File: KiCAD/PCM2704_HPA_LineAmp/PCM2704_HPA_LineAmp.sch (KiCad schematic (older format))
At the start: 10 parts, among them J1 PCM2704Board, U1 NJM4580

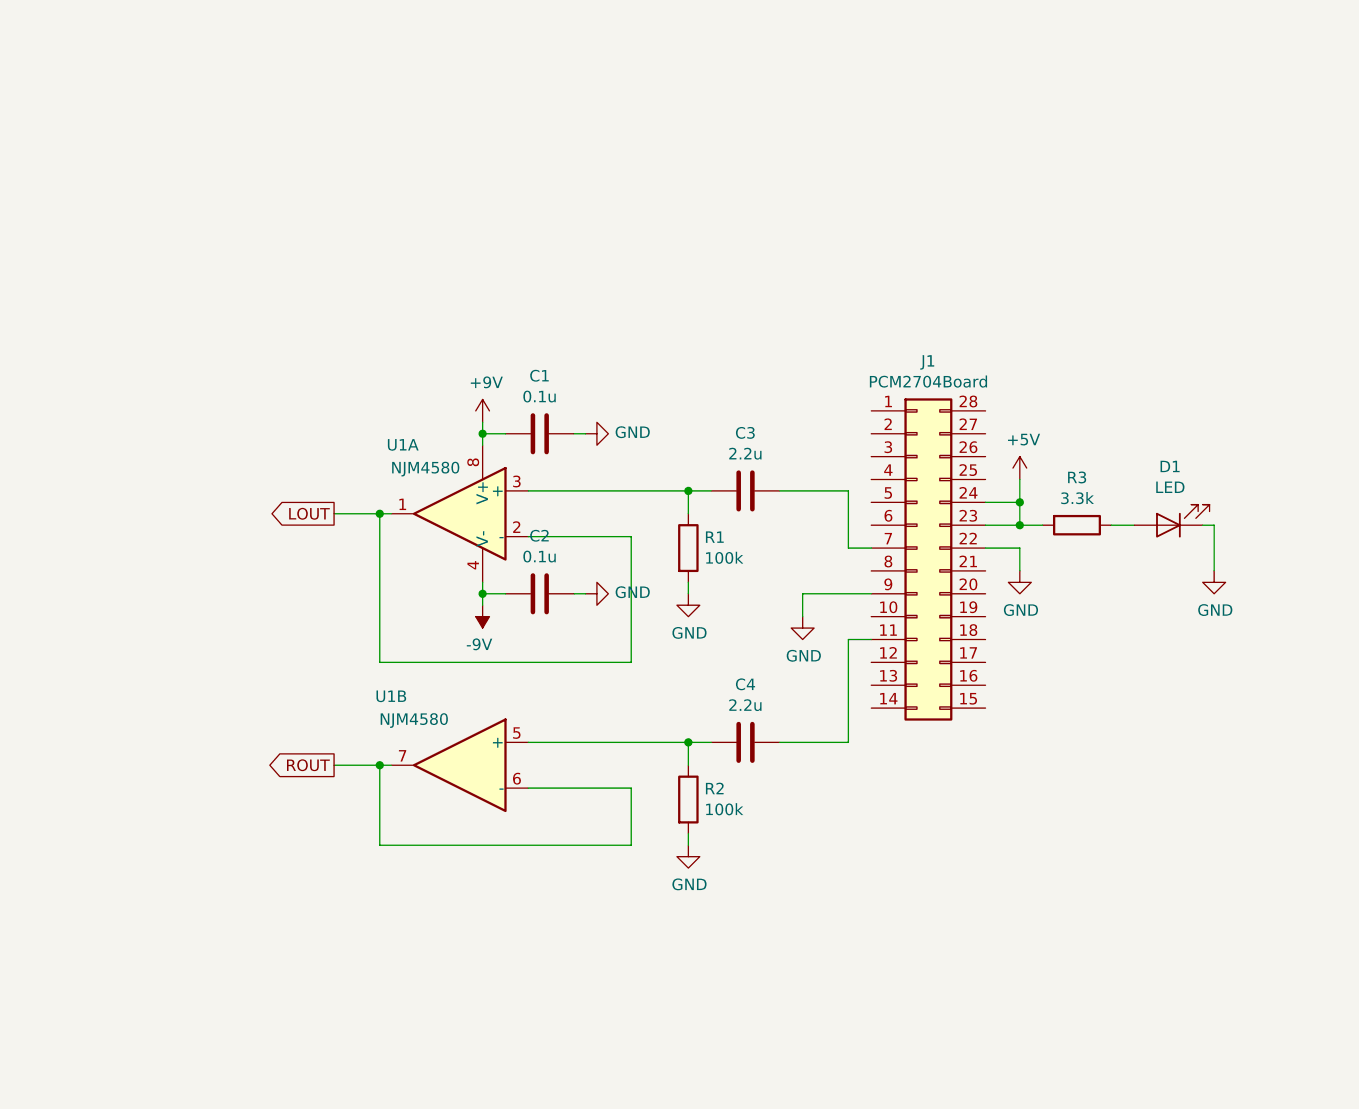
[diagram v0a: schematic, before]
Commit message: Add: PCM2704_LineAmp
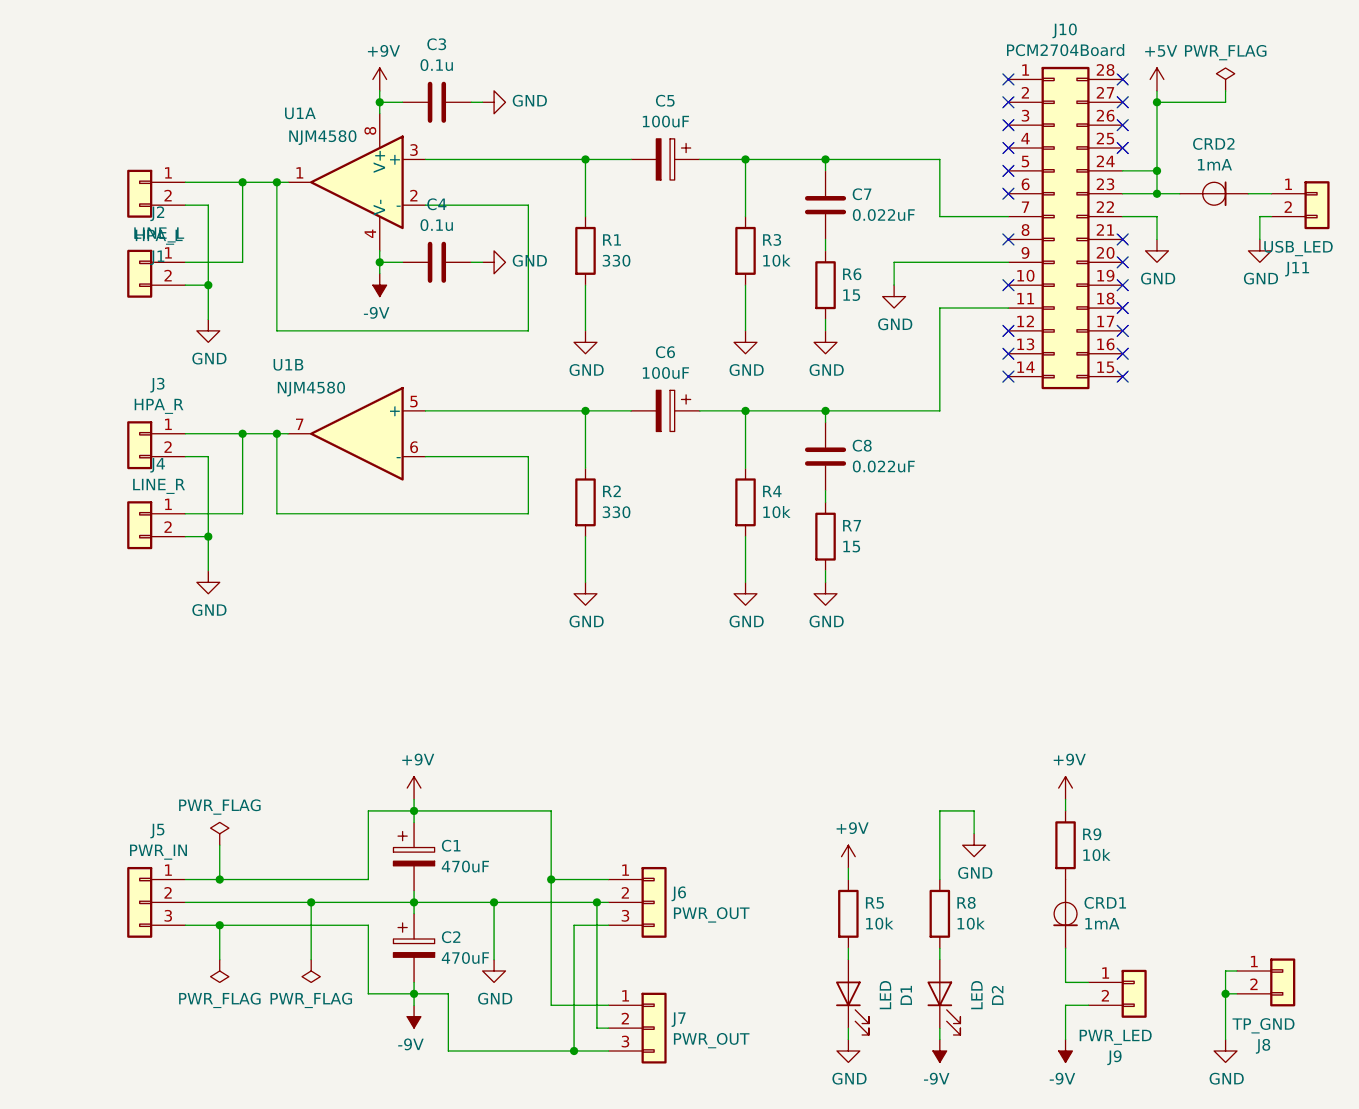
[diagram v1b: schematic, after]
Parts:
- removed C3, C4: 2.2u, symbol Device:C
- added C1, C2: 470uF, Capacitor_THT:CP_Radial_D10.0mm_P5.00mm, symbol Device:CP
- added C5, C6: 100uF, Capacitor_THT:CP_Radial_D8.0mm_P5.00mm, symbol Device:CP
- added C7, C8: 0.022uF, Capacitor_THT:C_Rect_L7.0mm_W2.0mm_P5.00mm, symbol Device:C
- added CRD1, CRD2: 1mA, Diode_THT:D_A-405_P7.62mm_Horizontal, symbol mylib:CRD
- added D2: LED, LED_THT:LED_D3.0mm, symbol Device:LED
- added J1: HPA_L, Connector_JST:JST_XH_B2B-XH-A_1x02_P2.50mm_Vertical, symbol Connector_Generic:Conn_01x02
- added J11: USB_LED, Connector_PinHeader_2.54mm:PinHeader_1x02_P2.54mm_Vertical, symbol Connector_Generic:Conn_01x02
- added J2: LINE_L, Connector_JST:JST_XH_B2B-XH-A_1x02_P2.50mm_Vertical, symbol Connector_Generic:Conn_01x02
- added J3: HPA_R, Connector_JST:JST_XH_B2B-XH-A_1x02_P2.50mm_Vertical, symbol Connector_Generic:Conn_01x02
- added J4: LINE_R, Connector_JST:JST_XH_B2B-XH-A_1x02_P2.50mm_Vertical, symbol Connector_Generic:Conn_01x02
- added J5: PWR_IN, Connector_JST:JST_XH_B3B-XH-A_1x03_P2.50mm_Vertical, symbol Connector_Generic:Conn_01x03
- added J6, J7: PWR_OUT, Connector_JST:JST_XH_B3B-XH-A_1x03_P2.50mm_Vertical, symbol Connector_Generic:Conn_01x03
- added J8: TP_GND, Connector_PinHeader_2.54mm:PinHeader_1x02_P2.54mm_Vertical, symbol Connector_Generic:Conn_01x02
- added J9: PWR_LED, Connector_PinHeader_2.54mm:PinHeader_1x02_P2.54mm_Vertical, symbol Connector_Generic:Conn_01x02
- added R4, R5, R8, R9: 10k, Resistor_THT:R_Axial_DIN0204_L3.6mm_D1.6mm_P7.62mm_Horizontal, symbol Device:R
- added R6, R7: 15, Resistor_THT:R_Axial_DIN0204_L3.6mm_D1.6mm_P7.62mm_Horizontal, symbol Device:R
- C3: renamed from C1; footprint (none) -> Capacitor_THT:C_Disc_D3.0mm_W1.6mm_P2.50mm
- C4: renamed from C2; footprint (none) -> Capacitor_THT:C_Disc_D3.0mm_W1.6mm_P2.50mm
- D1: footprint (none) -> LED_THT:LED_D3.0mm
- J10: renamed from J1; footprint (none) -> Package_DIP:DIP-28_W15.24mm
- R1, R2: value 100k -> 330; footprint (none) -> Resistor_THT:R_Axial_DIN0204_L3.6mm_D1.6mm_P7.62mm_Horizontal
- R3: value 3.3k -> 10k; footprint (none) -> Resistor_THT:R_Axial_DIN0204_L3.6mm_D1.6mm_P7.62mm_Horizontal
- U1: footprint (none) -> Package_DIP:DIP-8_W7.62mm_Socket
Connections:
- net +5V: now also CRD2.2 (A); no longer R3.2
- net +9V: now also C1.1, J5.1 (Pin_1), J6.1 (Pin_1), J7.1 (Pin_1), R5.1, R9.1
- net -9V: now also C2.2, D2.1 (K), J5.3 (Pin_3), J6.3 (Pin_3), J7.3 (Pin_3), J9.2 (Pin_2)
- net GND: now also R3.2, C1.2, C2.1, J1.2 (Pin_2), J11.2 (Pin_2), J2.2 (Pin_2), J3.2 (Pin_2), J4.2 (Pin_2), J5.2 (Pin_2), J6.2 (Pin_2), J7.2 (Pin_2), J8.1 (Pin_1), J8.2 (Pin_2), R4.2, R6.2, R7.2, R8.1
- net at J10.11 (Pin_11): now also C6.1, C8.1, R4.1
- net at J10.7 (Pin_7): now also R3.1, C5.1, C7.1
- net at D1.2 (A): now also R5.2; no longer R3.1
- net at R1.1, U1.3 (+): now also C5.2
- net at R2.1, U1.5 (+): now also C6.2
- net LOUT: no longer names the net of U1.1, U1.2 (-)
- net LOUT: now also J1.1 (Pin_1), J2.1 (Pin_1)
- net ROUT: no longer names the net of U1.6 (-), U1.7
- net ROUT: now also J3.1 (Pin_1), J4.1 (Pin_1)
- new net: C7.2, R6.1
- new net: C8.2, R7.1
- new net: CRD1.1 (K), J9.1 (Pin_1)
- new net: CRD1.2 (A), R9.2
- new net: D2.2 (A), R8.2
- new net: CRD2.1 (K), J11.1 (Pin_1)
- no-connect marks 0 -> 22
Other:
- moved on the sheet: C3, C4, J10, R1, R2, U1A, U1B

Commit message: Update: PCM2704_HPA_LineAmp board design
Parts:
- removed J5: PWR_IN, Connector_JST:JST_XH_B3B-XH-A_1x03_P2.50mm_Vertical, symbol Connector_Generic:Conn_01x03
- added J12: PWR-, Connector_JST:JST_XH_B2B-XH-A_1x02_P2.50mm_Vertical, symbol Connector_Generic:Conn_01x02
- added J5: PWR+, Connector_JST:JST_XH_B2B-XH-A_1x02_P2.50mm_Vertical, symbol Connector_Generic:Conn_01x02
- C4: footprint Capacitor_THT:C_Disc_D3.0mm_W1.6mm_P2.50mm -> Capacitor_THT:C_Disc_D4.3mm_W1.9mm_P5.00mm
- C5, C6: footprint Capacitor_THT:CP_Radial_D8.0mm_P5.00mm -> Capacitor_THT:CP_Radial_D7.5mm_P2.50mm
- CRD1, CRD2: value 1mA -> 10mA; footprint Diode_THT:D_A-405_P7.62mm_Horizontal -> Diode_THT:D_DO-35_SOD27_P7.62mm_Horizontal
- R1, R2: value 330 -> 3k3
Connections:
- net +9V: now also D1.2 (A), J5.1 (Pin_1); no longer R5.1
- net -9V: now also J12.2 (Pin_2)
- net GND: now also R5.2, J12.1 (Pin_1), J5.2 (Pin_2); no longer D1.1 (K)
- net at C5.2, R1.1: now also U1.5 (+); no longer U1.3 (+)
- net at C6.2, R2.1: now also U1.3 (+); no longer U1.5 (+)
- net at U1.1, U1.2 (-): now also J3.1 (Pin_1), J4.1 (Pin_1); no longer J1.1 (Pin_1), J2.1 (Pin_1)
- net at U1.6 (-), U1.7: now also J1.1 (Pin_1), J2.1 (Pin_1); no longer J3.1 (Pin_1), J4.1 (Pin_1)
- new net: D1.1 (K), R5.1
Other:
- moved on the sheet: D1, R5, U1A, U1B
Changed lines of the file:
@@
 encoding utf-8
 Sheet 1 1
-Title "PCM2074 Line Amp"
-Date "2019-11-06"
+Title "PCM2704 Line Amp"
+Date "2019-11-08"
 Rev "Rev. A"
 Comp "PNPN Manufactory"
@@
 P 4900 2250
 F 0 "R1" H 4970 2296 50  0000 L CNN
-F 1 "330" H 4970 2205 50  0000 L CNN
+F 1 "3k3" H 4970 2205 50  0000 L CNN
 F 2 "Resistor_THT:R_Axial_DIN0204_L3.6mm_D1.6mm_P7.62mm_Horizontal" V 4830 2250 50  0001 C CNN
 F 3 "~" H 4900 2250 50  0001 C CNN
@@
 P 4900 3350
 F 0 "R2" H 4970 3396 50  0000 L CNN
-F 1 "330" H 4970 3305 50  0000 L CNN
+F 1 "3k3" H 4970 3305 50  0000 L CNN
 F 2 "Resistor_THT:R_Axial_DIN0204_L3.6mm_D1.6mm_P7.62mm_Horizontal" V 4830 3350 50  0001 C CNN
 F 3 "~" H 4900 3350 50  0001 C CNN
@@
 L Amplifier_Operational:NJM4580 U1
 U 1 1 5DA27AD1
+P 3900 3050
+F 0 "U1" H 4150 3350 50  0000 C CNN
+F 1 "NJM4580" H 4050 3250 50  0000 C CNN
+F 2 "Package_DIP:DIP-8_W7.62mm_Socket" H 3900 3050 50  0001 C CNN
+F 3 "http://www.njr.com/semicon/PDF/NJM4580_E.pdf" H 3900 3050 50  0001 C CNN
+	1    3900 3050
+	-1   0    0    -1
+$EndComp
+$Comp
+L Amplifier_Operational:NJM4580 U1
+U 2 1 5DA2AA3E
 P 3900 1950
-F 0 "U1" H 4150 2250 50  0000 C CNN
-F 1 "NJM4580" H 4050 2150 50  0000 C CNN
+F 0 "U1" H 4200 2250 50  0000 C CNN
+F 1 "NJM4580" H 4100 2150 50  0000 C CNN
 F 2 "Package_DIP:DIP-8_W7.62mm_Socket" H 3900 1950 50  0001 C CNN
 F 3 "http://www.njr.com/semicon/PDF/NJM4580_E.pdf" H 3900 1950 50  0001 C CNN
-	1    3900 1950
-	-1   0    0    -1
-$EndComp
-$Comp
-L Amplifier_Operational:NJM4580 U1
-U 2 1 5DA2AA3E
-P 3900 3050
-F 0 "U1" H 4200 3350 50  0000 C CNN
-F 1 "NJM4580" H 4100 3250 50  0000 C CNN
-F 2 "Package_DIP:DIP-8_W7.62mm_Socket" H 3900 3050 50  0001 C CNN
-F 3 "http://www.njr.com/semicon/PDF/NJM4580_E.pdf" H 3900 3050 50  0001 C CNN
-	2    3900 3050
+	2    3900 1950
 	-1   0    0    -1
 $EndComp
@@
 F 0 "C4" V 3998 2300 50  0000 C CNN
 F 1 "0.1u" V 4089 2300 50  0000 C CNN
-F 2 "Capacitor_THT:C_Disc_D3.0mm_W1.6mm_P2.50mm" H 4288 2150 50  0001 C CNN
+F 2 "Capacitor_THT:C_Disc_D4.3mm_W1.9mm_P5.00mm" H 4288 2150 50  0001 C CNN
 F 3 "~" H 4250 2300 50  0001 C CNN
 	1    4250 2300
@@
 F 0 "C5" V 4995 1850 50  0000 C CNN
 F 1 "100uF" V 5086 1850 50  0000 C CNN
-F 2 "Capacitor_THT:CP_Radial_D8.0mm_P5.00mm" H 5288 1700 50  0001 C CNN
+F 2 "Capacitor_THT:CP_Radial_D7.5mm_P2.50mm" H 5288 1700 50  0001 C CNN
 F 3 "~" H 5250 1850 50  0001 C CNN
 	1    5250 1850
@@
 F 0 "C6" V 4995 2950 50  0000 C CNN
 F 1 "100uF" V 5086 2950 50  0000 C CNN
-F 2 "Capacitor_THT:CP_Radial_D8.0mm_P5.00mm" H 5288 2800 50  0001 C CNN
+F 2 "Capacitor_THT:CP_Radial_D7.5mm_P2.50mm" H 5288 2800 50  0001 C CNN
 F 3 "~" H 5250 2950 50  0001 C CNN
 	1    5250 2950
@@
 U 1 1 5DC7B009
 P 2950 1950
-F 0 "J1" H 2868 1625 50  0000 C CNN
-F 1 "HPA_L" H 2868 1716 50  0000 C CNN
+F 0 "J1" H 3100 2000 50  0000 C CNN
+F 1 "HPA_L" H 2900 2050 50  0000 C CNN
 F 2 "Connector_JST:JST_XH_B2B-XH-A_1x02_P2.50mm_Vertical" H 2950 1950 50  0001 C CNN
 F 3 "~" H 2950 1950 50  0001 C CNN
@@
 U 1 1 5DC7B7CB
 P 2950 2300
-F 0 "J2" H 2868 2517 50  0000 C CNN
+F 0 "J2" H 3100 2350 50  0000 C CNN
 F 1 "LINE_L" H 2868 2426 50  0000 C CNN
 F 2 "Connector_JST:JST_XH_B2B-XH-A_1x02_P2.50mm_Vertical" H 2950 2300 50  0001 C CNN
@@
 U 1 1 5DC7C23E
 P 2950 3050
-F 0 "J3" H 2868 3267 50  0000 C CNN
+F 0 "J3" H 3100 3100 50  0000 C CNN
 F 1 "HPA_R" H 2868 3176 50  0000 C CNN
 F 2 "Connector_JST:JST_XH_B2B-XH-A_1x02_P2.50mm_Vertical" H 2950 3050 50  0001 C CNN
@@
 U 1 1 5DC7CA20
 P 2950 3400
-F 0 "J4" H 2868 3617 50  0000 C CNN
+F 0 "J4" H 3100 3450 50  0000 C CNN
 F 1 "LINE_R" H 2868 3526 50  0000 C CNN
 F 2 "Connector_JST:JST_XH_B2B-XH-A_1x02_P2.50mm_Vertical" H 2950 3400 50  0001 C CNN
@@
 	7900 2100 7850 2100
 $Comp
-L Connector_Generic:Conn_01x03 J5
-U 1 1 5DD6183F
-P 2950 5100
-F 0 "J5" H 2868 5417 50  0000 C CNN
-F 1 "PWR_IN" H 2868 5326 50  0000 C CNN
-F 2 "Connector_JST:JST_XH_B3B-XH-A_1x03_P2.50mm_Vertical" H 2950 5100 50  0001 C CNN
-F 3 "~" H 2950 5100 50  0001 C CNN
-	1    2950 5100
-	-1   0    0    -1
-$EndComp
-$Comp
 L Connector_Generic:Conn_01x03 J6
 U 1 1 5DD62FDF
@@
 $EndComp
 Wire Wire Line
-	3150 5000 3300 5000
+	2850 5000 3300 5000
 Wire Wire Line
 	3950 5000 3950 4700
@@
 	4150 5150 4150 5100
 Wire Wire Line
-	3150 5200 3300 5200
-Wire Wire Line
 	3950 5200 3950 5500
 Wire Wire Line
@@
 	4150 5500 4150 5450
 Wire Wire Line
-	3150 5100 3700 5100
+	2850 5100 3050 5100
 Connection ~ 4150 5100
 Wire Wire Line
@@
 L Device:LED D1
 U 1 1 5DE43980
-P 6050 5500
-F 0 "D1" H 6043 5245 50  0000 C CNN
-F 1 "LED" H 6043 5336 50  0000 C CNN
-F 2 "LED_THT:LED_D3.0mm" H 6050 5500 50  0001 C CNN
-F 3 "~" H 6050 5500 50  0001 C CNN
-	1    6050 5500
+P 6050 5150
+F 0 "D1" H 6043 4895 50  0000 C CNN
+F 1 "LED" H 6043 4986 50  0000 C CNN
+F 2 "LED_THT:LED_D3.0mm" H 6050 5150 50  0001 C CNN
+F 3 "~" H 6050 5150 50  0001 C CNN
+	1    6050 5150
 	0    -1   -1   0
 $EndComp
@@
 P 7000 5150
 F 0 "CRD1" V 7046 5071 50  0000 R CNN
-F 1 "1mA" V 6955 5071 50  0000 R CNN
-F 2 "Diode_THT:D_A-405_P7.62mm_Horizontal" H 7000 5150 50  0001 C CNN
+F 1 "10mA" V 6955 5071 50  0000 R CNN
+F 2 "Diode_THT:D_DO-35_SOD27_P7.62mm_Horizontal" H 7000 5150 50  0001 C CNN
 F 3 "~" H 7000 5150 50  0001 C CNN
 	1    7000 5150
@@
 P 7650 2000
 F 0 "CRD2" H 7650 1784 50  0000 C CNN
-F 1 "1mA" H 7650 1875 50  0000 C CNN
-F 2 "Diode_THT:D_A-405_P7.62mm_Horizontal" H 7650 2000 50  0001 C CNN
+F 1 "10mA" H 7650 1875 50  0000 C CNN
+F 2 "Diode_THT:D_DO-35_SOD27_P7.62mm_Horizontal" H 7650 2000 50  0001 C CNN
 F 3 "~" H 7650 2000 50  0001 C CNN
 	1    7650 2000
@@
 L Device:R R5
 U 1 1 5DD2A85D
-P 6050 5150
-F 0 "R5" H 6120 5196 50  0000 L CNN
-F 1 "10k" H 6120 5105 50  0000 L CNN
-F 2 "Resistor_THT:R_Axial_DIN0204_L3.6mm_D1.6mm_P7.62mm_Horizontal" V 5980 5150 50  0001 C CNN
-F 3 "~" H 6050 5150 50  0001 C CNN
-	1    6050 5150
+P 6050 5500
+F 0 "R5" H 6120 5546 50  0000 L CNN
+F 1 "10k" H 6120 5455 50  0000 L CNN
+F 2 "Resistor_THT:R_Axial_DIN0204_L3.6mm_D1.6mm_P7.62mm_Horizontal" V 5980 5500 50  0001 C CNN
+F 3 "~" H 6050 5500 50  0001 C CNN
+	1    6050 5500
 	1    0    0    -1
 $EndComp
@@
 	4300 5750 4850 5750
 Connection ~ 4850 5750
+$Comp
+L Connector_Generic:Conn_01x02 J5
+U 1 1 5DCA298D
+P 2650 5000
+F 0 "J5" H 2800 5050 50  0000 C CNN
+F 1 "PWR+" H 2568 5126 50  0000 C CNN
+F 2 "Connector_JST:JST_XH_B2B-XH-A_1x02_P2.50mm_Vertical" H 2650 5000 50  0001 C CNN
+F 3 "~" H 2650 5000 50  0001 C CNN
+	1    2650 5000
+	-1   0    0    -1
+$EndComp
+$Comp
+L Connector_Generic:Conn_01x02 J12
+U 1 1 5DCA3545
+P 2650 5450
+F 0 "J12" H 2800 5500 50  0000 C CNN
+F 1 "PWR-" H 2568 5576 50  0000 C CNN
+F 2 "Connector_JST:JST_XH_B2B-XH-A_1x02_P2.50mm_Vertical" H 2650 5450 50  0001 C CNN
+F 3 "~" H 2650 5450 50  0001 C CNN
+	1    2650 5450
+	-1   0    0    1
+$EndComp
+Wire Wire Line
+	2850 5450 3050 5450
+Wire Wire Line
+	3050 5450 3050 5100
+Connection ~ 3050 5100
+Wire Wire Line
+	3050 5100 3700 5100
+Wire Wire Line
+	2850 5350 2900 5350
+Wire Wire Line
+	2900 5350 2900 5200
+Wire Wire Line
+	2900 5200 3300 5200
 $EndSCHEMATC

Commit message: Update: PCM2704_HPA_LineAmp board design
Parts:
- removed CRD2: 10mA, Diode_THT:D_DO-35_SOD27_P7.62mm_Horizontal, symbol mylib:CRD
- added R10: 3k3, Resistor_THT:R_Axial_DIN0204_L3.6mm_D1.6mm_P7.62mm_Horizontal, symbol Device:R
- CRD1: value 10mA -> 5mA
- renumbered J5 to J1, J9 to J10, J8 to J11, J11 to J12, J12 to J2, J1 to J3, J2 to J4, J3 to J5, J4 to J6, J6 to J7, J7 to J8, J10 to J9, R6 to R5, R7 to R6, R5 to R7
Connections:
- net +5V: now also R10.2
- net at J12.1 (Pin_1): now also R10.1

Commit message: Add: Case design
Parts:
- removed J1: PWR+, Connector_JST:JST_XH_B2B-XH-A_1x02_P2.50mm_Vertical, symbol Connector_Generic:Conn_01x02
- removed J2: PWR-, Connector_JST:JST_XH_B2B-XH-A_1x02_P2.50mm_Vertical, symbol Connector_Generic:Conn_01x02
- removed R9: 10k, Resistor_THT:R_Axial_DIN0204_L3.6mm_D1.6mm_P7.62mm_Horizontal, symbol Device:R
- added J1: PWR_IN, Connector_JST:JST_XH_B3B-XH-A_1x03_P2.50mm_Vertical, symbol Connector_Generic:Conn_01x03
- R7, R8: value 10k -> 4k7
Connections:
- net +9V: now also CRD1.2 (A), J1.1 (Pin_1)
- net -9V: now also J1.3 (Pin_3)
- net GND: now also J1.2 (Pin_2)
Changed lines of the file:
@@
 Sheet 1 1
 Title "PCM2704 Line Amp"
-Date "2019-11-12"
+Date "2019-11-15"
 Rev "Rev. A"
 Comp "PNPN Manufactory"
@@
 $EndComp
 Wire Wire Line
-	2850 5000 3300 5000
+	3150 5000 3300 5000
 Wire Wire Line
 	3950 5000 3950 4700
@@
 Wire Wire Line
 	4150 5500 4150 5450
-Wire Wire Line
-	2850 5100 3050 5100
 Connection ~ 4150 5100
 Wire Wire Line
@@
 L power:+9V #PWR021
 U 1 1 5DC50056
-P 7000 4650
-F 0 "#PWR021" H 7000 4500 50  0001 C CNN
-F 1 "+9V" H 7015 4823 50  0000 C CNN
-F 2 "" H 7000 4650 50  0001 C CNN
-F 3 "" H 7000 4650 50  0001 C CNN
-	1    7000 4650
+P 7000 4950
+F 0 "#PWR021" H 7000 4800 50  0001 C CNN
+F 1 "+9V" H 7015 5123 50  0000 C CNN
+F 2 "" H 7000 4950 50  0001 C CNN
+F 3 "" H 7000 4950 50  0001 C CNN
+	1    7000 4950
 	1    0    0    -1
 $EndComp
@@
 $EndComp
 Wire Wire Line
-	7000 4650 7000 4700
+	7000 4950 7000 5000
 Wire Wire Line
 	7000 5300 7000 5450
@@
 Wire Wire Line
 	7000 5550 7000 5700
-$Comp
-L Device:R R9
-U 1 1 5DCB46AD
-P 7000 4850
-F 0 "R9" H 7070 4896 50  0000 L CNN
-F 1 "10k" H 7070 4805 50  0000 L CNN
-F 2 "Resistor_THT:R_Axial_DIN0204_L3.6mm_D1.6mm_P7.62mm_Horizontal" V 6930 4850 50  0001 C CNN
-F 3 "~" H 7000 4850 50  0001 C CNN
-	1    7000 4850
-	1    0    0    -1
-$EndComp
 Wire Wire Line
 	7850 2100 7850 2200
@@
 P 6050 5500
 F 0 "R7" H 6120 5546 50  0000 L CNN
-F 1 "10k" H 6120 5455 50  0000 L CNN
+F 1 "4k7" H 6120 5455 50  0000 L CNN
 F 2 "Resistor_THT:R_Axial_DIN0204_L3.6mm_D1.6mm_P7.62mm_Horizontal" V 5980 5500 50  0001 C CNN
 F 3 "~" H 6050 5500 50  0001 C CNN
@@
 P 6450 5150
 F 0 "R8" H 6520 5196 50  0000 L CNN
-F 1 "10k" H 6520 5105 50  0000 L CNN
+F 1 "4k7" H 6520 5105 50  0000 L CNN
 F 2 "Resistor_THT:R_Axial_DIN0204_L3.6mm_D1.6mm_P7.62mm_Horizontal" V 6380 5150 50  0001 C CNN
 F 3 "~" H 6450 5150 50  0001 C CNN
@@
 	4300 5750 4850 5750
 Connection ~ 4850 5750
-$Comp
-L Connector_Generic:Conn_01x02 J1
-U 1 1 5DCA298D
-P 2650 5000
-F 0 "J1" H 2800 5050 50  0000 C CNN
-F 1 "PWR+" H 2568 5126 50  0000 C CNN
-F 2 "Connector_JST:JST_XH_B2B-XH-A_1x02_P2.50mm_Vertical" H 2650 5000 50  0001 C CNN
-F 3 "~" H 2650 5000 50  0001 C CNN
-	1    2650 5000
-	-1   0    0    -1
-$EndComp
-$Comp
-L Connector_Generic:Conn_01x02 J2
-U 1 1 5DCA3545
-P 2650 5450
-F 0 "J2" H 2800 5500 50  0000 C CNN
-F 1 "PWR-" H 2568 5576 50  0000 C CNN
-F 2 "Connector_JST:JST_XH_B2B-XH-A_1x02_P2.50mm_Vertical" H 2650 5450 50  0001 C CNN
-F 3 "~" H 2650 5450 50  0001 C CNN
-	1    2650 5450
-	-1   0    0    1
-$EndComp
-Wire Wire Line
-	2850 5450 3050 5450
-Wire Wire Line
-	3050 5450 3050 5100
-Connection ~ 3050 5100
-Wire Wire Line
-	3050 5100 3700 5100
-Wire Wire Line
-	2850 5350 2900 5350
-Wire Wire Line
-	2900 5350 2900 5200
-Wire Wire Line
-	2900 5200 3300 5200
 $Comp
 L Device:R R10
@@
 	0    1    1    0
 $EndComp
+$Comp
+L Connector_Generic:Conn_01x03 J1
+U 1 1 5DD00DFB
+P 2950 5100
+F 0 "J1" H 3030 5142 50  0000 L CNN
+F 1 "PWR_IN" H 3030 5051 50  0000 L CNN
+F 2 "Connector_JST:JST_XH_B3B-XH-A_1x03_P2.50mm_Vertical" H 2950 5100 50  0001 C CNN
+F 3 "~" H 2950 5100 50  0001 C CNN
+	1    2950 5100
+	-1   0    0    -1
+$EndComp
+Wire Wire Line
+	3150 5100 3700 5100
+Wire Wire Line
+	3150 5200 3300 5200
 $EndSCHEMATC
